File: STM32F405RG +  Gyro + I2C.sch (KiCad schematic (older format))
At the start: 41 parts

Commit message: Added more things to circuit
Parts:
- added C_small?: 1uF, symbol Device:C_Small
- added C_small?: 10nF, symbol Device:C_Small
- added J?: Conn_01x04, symbol Connector_Generic:Conn_01x04
- added L?: 47nH, symbol Device:L_Small
- added R?: 22, symbol Device:R_Small
- added R?: 10k, symbol Device:R_Small
- added SW?: SW_SPDT, symbol Switch:SW_SPDT
- U?: symbol Power_Protection:USBLC6-2SC6 -> STM32F405RG-+--Gyro-+-I2C-rescue:USBLC6-2SC6-Power_Protection
- U?: symbol OllieKiCadLibrary:MP2359DJ-LF-Z -> STM32F405RG-+--Gyro-+-I2C-rescue:MP2359DJ-LF-Z-OllieKiCadLibrary
- renumbered CVCAP1_Ceramic to VCAP1_Ceramic, CVCAP2_Ceramic to VCAP2_Ceramic
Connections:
- net labels added: +3.3VA, USART_RX, USART_TX
- wire segments 136 -> 152
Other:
- note added: "AD0 (Address select pin) which is a I2C slave address select pin. \nWon't need since we won't connect two of the same gyros to the same I2C.\n\nINT (interrupt) pin which is an interrupt digital output pin and used to \ngive indication to the MCU that data is available to read from the MPU6050.\n\nFSYNC is used to sync the MP6050 with a videocamera etc. \nIf unused, connect to ground according to 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"
- note added: "Analog power supply filtering"
- note added: "Boot mode"
- note added: "Crystal Oscillator"
- note added: "Current limiting resistor \nto prevent burning up MCU \nif accidentally shorted."
- note added: "Decoupling capacitors were recommended \nin the datasheet for STM32F405."
- note added: "Decoupling capacitors were recommended \nin the datasheet for STM32F405. Should be \nplaced close to the MCU."
- note added: "I2C Pull-up resistors"
- note added: "ISO 7816 Interface\nVCC can be 5V or 3.3V"
- note added: "MCU STM32F405"
- note added: "Power Supply & Filtering\n"
- note added: "Pull-up resistors are needed for I2C to \nensure the logical state. \nShould be in range 2k to 10k"
- note added: "The Schottky diode acts as an OR-gate. When the 12V power supply is connected, \nthere is 5V on the anode(+) and 12V on the cathode(-) resulting in the diode not conducting. \nWhen there is only 5V supplied from the USB, there is 5V on the anode(+) and approx. 4.5V on the cathode(-), \nmaking the diode conduct properly. \n"
- note added: "The inductor together with the capacitors in parallel \nform a low pass filter with Fc = 730.484 kHz"
- note added: "USART"
- note added: "USB B Mini"
- note removed: "AD0 (Address select pin) which is a I2C slave address select pin. \nWon't need since we wont connect two of the same gyros to the same I2C.\n\nINT (interrupt) pin which is an interrupt digital output pin and used to \ngive indication to the MCU that data is available to read from the MPU6050.\n\nFSYNC is used to sync the MP6050 with a videocamera etc. \nIf unused, connect to ground according to d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"
- note removed: "Pull-up resistors are needed for I2C to ensure the logical state. \nShould be in range 2k to 10k"
- note removed: "The Schottky diode acts as an OR-gate. When the 12V power supply is connected, \nthere is 5V on the anode(+) and 12V on the cathode(-) resulting in the diode not conducting. \nWhen there only is 5V supplied from the USB, there is 5V on the anode(+) and ~4.5V on the cathode(-), \nmaking the diode conduct properly. \n"
- moved on the sheet: C?, CPower_Ceramic, C_small, C_small?, Ceramic_10, Ceramic_20, Ceramic_VDD, Ceramic_VLOGIC, D?, F?, FB?, J?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

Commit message: Added annotations
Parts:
- removed Ceramic_VLOGIC: 10nF, symbol Device:C_Small
- removed R?: 100k, symbol Device:R_Small
- removed R?: 150k, symbol Device:R_Small
- removed R?: R_Small, symbol Device:R_Small
- removed U?: MPU-6050, Sensor_Motion:InvenSense_QFN-24_4x4mm_P0.5mm, symbol Sensor_Motion:MPU-6050
- added R10, R11, R9: 22, symbol Device:R_Small
- added R12: 10k, symbol Device:R_Small
- added R4: 15k, symbol Device:R_Small
- added R6: 270, symbol Device:R_Small
- added U2: MPU-6000, Sensor_Motion:InvenSense_QFN-24_4x4mm_P0.5mm, symbol Sensor_Motion:MPU-6000
- J1: renamed from J?; symbol STM32F405RG-+--Gyro-+-I2C-rescue:USB_B_Mini-Connector -> STM32F405RG-+--Gyro-+-I2C-rescue:USB_B_Mini-Connector-STM32F405RG-+--Gyro-+-I2C-rescue-STM32F405RG-+--Gyro-+-I2C-rescue
- R2: renamed from R?; value R_Small -> 47k
- R5: renamed from R?; value 10k -> 1k
- U1: renamed from U?; symbol STM32F405RG-+--Gyro-+-I2C-rescue:MP2359DJ-LF-Z-OllieKiCadLibrary -> STM32F405RG-+--Gyro-+-I2C-rescue:MP2359DJ-LF-Z-OllieKiCadLibrary-STM32F405RG-+--Gyro-+-I2C-rescue
- U3: renamed from U?; symbol STM32F405RG-+--Gyro-+-I2C-rescue:USBLC6-2SC6-Power_Protection -> STM32F405RG-+--Gyro-+-I2C-rescue:USBLC6-2SC6-Power_Protection-STM32F405RG-+--Gyro-+-I2C-rescue
- gave numbers to parts that had none: 31
- renumbered VCAP2_Ceramic to C10, CPower_Ceramic to C11, C_small to C12, Ceramic_VDD to C6, Ceramic_10 to C7, Ceramic_20 to C8, VCAP1_Ceramic to C9
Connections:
- net labels added: BOOT1
- net labels removed: +1V8
- wire segments 152 -> 158
- no-connect marks 7 -> 6
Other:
- note added: "C = 2 * (C_load - C_stray)"
- note added: "Cap on pin 10, 20 and Vdd needs to be Ceramic"
- note added: "ESD protection for USB"
- note added: "FB (Feedback voltage) needs to be between 0.790 V and 0.830 V\n\n(15k+270)/(47k+15k+270) * 3.3V = 0.80923 V"
- note added: "Gyroscope MPU6000"
- note added: "INT (interrupt) pin which is an interrupt digital output pin and used to \ngive indication to the MCU that data is available to read from the MPU6000.\n\nFSYNC is used to sync the MP6000 with a videocamera etc. \nIf unused, connect to ground according to datasheet. \n\nCLKIN is optional external reference clock input. If unused, connect to ground according to datasheet."
- note added: "VCAP1, VCAP2 and Decoupling capacitors needs to be ceramic"
- note removed: "AD0 (Address select pin) which is a I2C slave address select pin. \nWon't need since we won't connect two of the same gyros to the same I2C.\n\nINT (interrupt) pin which is an interrupt digital output pin and used to \ngive indication to the MCU that data is available to read from the MPU6050.\n\nFSYNC is used to sync the MP6050 with a videocamera etc. \nIf unused, connect to ground according to 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"
- note removed: "Gyroscope MPU6050"
- note removed: "VLOGIC voltage"
- moved on the sheet: C6, C7, C8, J2, J3, R8

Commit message: Started PCB layout
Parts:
- removed J1: USB_B_Mini, symbol STM32F405RG-+--Gyro-+-I2C-rescue:USB_B_Mini-Connector-STM32F405RG-+--Gyro-+-I2C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
- added C19: 100nF, Capacitor_SMD:C_0402_1005Metric, symbol Device:C_Small
- added D4, D5, D6, D7: BLUE_LED, LED_SMD:LED_0603_1608Metric, symbol Device:LED
- added D8: YELLOW_LED, LED_SMD:LED_0603_1608Metric, symbol Device:LED
- added J1: USB_B_Micro, USB Footprint Library:USB_Micro-B_GCT_USB3076-30-A, symbol Connector:USB_B_Micro
- added J4: 12V_CONN, TerminalBlock_Phoenix:TerminalBlock_Phoenix_PT-1,5-2-5.0-H_1x02_P5.00mm_Horizontal, symbol Connector:Screw_Terminal_01x02
- added R16, R17, R18, R19: 1.5k, Resistor_SMD:R_0402_1005Metric, symbol Device:R_Small
- added R20: 1k, Resistor_SMD:R_0402_1005Metric, symbol Device:R_Small
- C1, C3: footprint (none) -> Capacitor_SMD:C_1206_3216Metric
- C10, C11, C2, C9: footprint (none) -> Capacitor_SMD:C_0603_1608Metric
- C12, C13, C14, C15, C16, C17, C18, C4, C5, C8: footprint (none) -> Capacitor_SMD:C_0402_1005Metric
- C6, C7: value 0.1uF -> 100nF; footprint (none) -> Capacitor_SMD:C_0402_1005Metric
- D1: footprint (none) -> Diode_SMD:D_SOD-123
- D2: value B230A -> B5819W; footprint (none) -> Diode_SMD:D_SOD-123
- D3: footprint (none) -> LED_SMD:LED_0603_1608Metric
- F1: footprint (none) -> Fuse:Fuse_1206_3216Metric
- FB1: value 600 @ 600Mhz -> 600 @ 100Mhz; footprint (none) -> Inductor_SMD:L_0805_2012Metric
- J2: value Conn_01x04 -> USART_CONN; footprint (none) -> Connector_Molex:Molex_PicoBlade_53048-0410_1x04_P1.25mm_Horizontal
- J3: value Conn_02x05_Odd_Even -> SWD_CONN; footprint (none) -> Connector_PinSocket_1.27mm:PinSocket_2x05_P1.27mm_Vertical_SMD
- L1: footprint (none) -> Inductor_SMD:L_Sunlord_MWSA0518_5.4x5.2mm
- L2: value 47nH -> 39nH; footprint (none) -> Inductor_SMD:L_0402_1005Metric
- Q1: value Q_PMOS_GSD -> AO3401A; footprint (none) -> Package_TO_SOT_SMD:SOT-23
- R1, R2, R3, R4, R5, R6: footprint (none) -> Resistor_SMD:R_0603_1608Metric
- R10, R11, R12, R13, R14, R15, R7, R8, R9: footprint (none) -> Resistor_SMD:R_0402_1005Metric
- SW1: footprint (none) -> Button_Switch_SMD:SW_SPDT_PCM12
- U1: footprint (none) -> Package_TO_SOT_SMD:SOT-23-6; symbol STM32F405RG-+--Gyro-+-I2C-rescue:MP2359DJ-LF-Z-OllieKiCadLibrary-STM32F405RG-+--Gyro-+-I2C-rescue -> STM32F405RG-+--Gyro-+-I2C-rescue:MP2359DJ-LF-Z-OllieKiCadLibrary-STM32F405RG-+--Gyro-+-I2C-rescue-STM32F405RG-+--Gyro-+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
- U3: symbol STM32F405RG-+--Gyro-+-I2C-rescue:USBLC6-2SC6-Power_Protection-STM32F405RG-+--Gyro-+-I2C-rescue -> STM32F405RG-+--Gyro-+-I2C-rescue:USBLC6-2SC6-Power_Protection-STM32F405RG-+--Gyro-+-I2C-rescue-STM32F405RG-+--Gyro-+-I2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
- Y1: footprint (none) -> Crystal:Crystal_SMD_3225-4Pin_3.2x2.5mm
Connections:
- net +12V: now also J4.1 (Pin_1)
- net +3V3: now also C19.1, R16.1, R17.1, R18.1, R19.1
- net +5V: now also J1.1 (VBUS)
- net GND: now also C19.2, J1.5 (GND), J4.2 (Pin_2), R20.2
- net USB_CONN_D+: now also J1.3 (D+)
- net USB_CONN_D-: now also J1.2 (D-)
- net TIM2_CH1: now reaches U4.14 (PA0)
- net TIM2_CH1: now also D4.1 (K)
- net TIM2_CH2: now reaches U4.15 (PA1)
- net TIM2_CH2: now also D5.1 (K)
- net TIM2_CH3: now reaches U4.16 (PA2)
- net TIM2_CH3: now also D6.1 (K)
- net TIM2_CH4: now reaches U4.17 (PA3)
- net TIM2_CH4: now also D7.1 (K)
- net LED: now reaches U4.53 (PC12)
- net LED: now also D8.2 (A)
- new net: D4.2 (A), R16.2
- new net: D5.2 (A), R17.2
- new net: D6.2 (A), R18.2
- new net: D7.2 (A), R19.2
- new net: D8.1 (K), R20.1
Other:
- note added: "PWM LED"
- note added: "The inductor together with the capacitors in parallel \nform a low pass filter with Fc = \n"
- note added: "USB B Micro"
- note removed: "The inductor together with the capacitors in parallel \nform a low pass filter with Fc = 730.484 kHz"
- note removed: "USB B Mini"

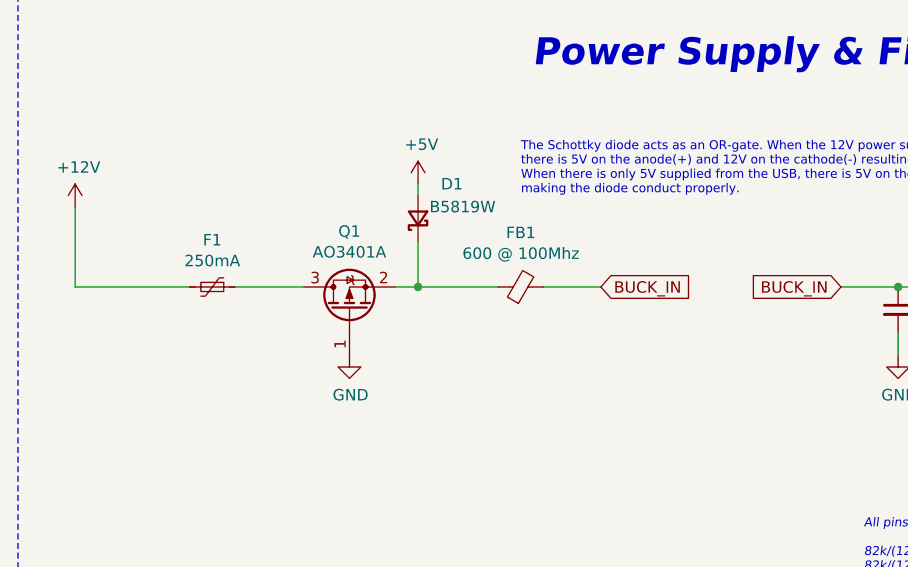
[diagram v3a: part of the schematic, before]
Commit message: Changed power supply layout
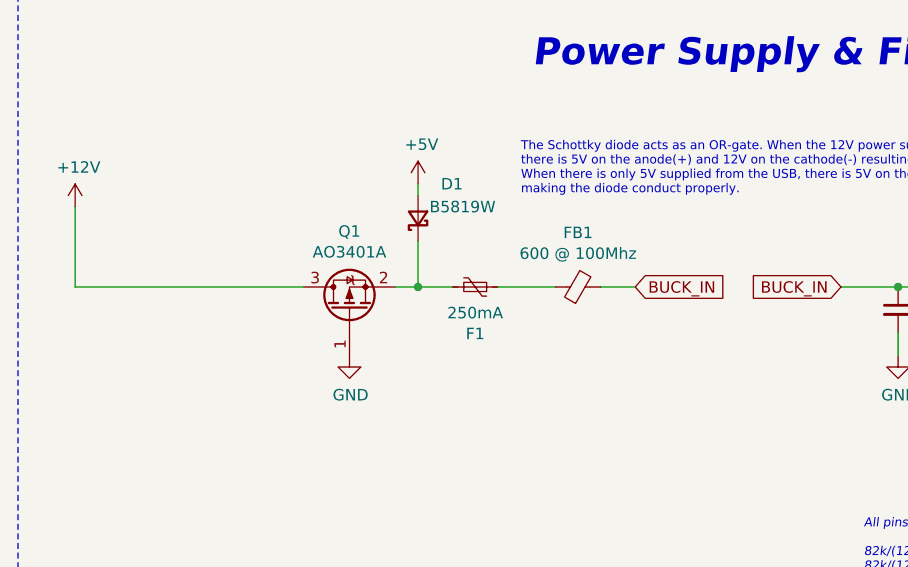
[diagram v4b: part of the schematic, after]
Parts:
- C7, C8: footprint Capacitor_SMD:C_0402_1005Metric -> Capacitor_SMD:C_0603_1608Metric
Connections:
- net +12V: now also Q1.3 (D); no longer F1.2
- net at F1.1: now also FB1.1; no longer Q1.3 (D)
- net at D1.1 (K), Q1.2 (S): now also F1.2; no longer FB1.1
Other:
- moved on the sheet: FB1
